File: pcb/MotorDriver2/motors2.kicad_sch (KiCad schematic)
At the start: 22 parts, among them Q2 IRLZ44NSTRLPBF, Q3 IRLZ44NSTRLPBF, Q4 IRLZ44NSTRLPBF, Q5 IRLZ44NSTRLPBF

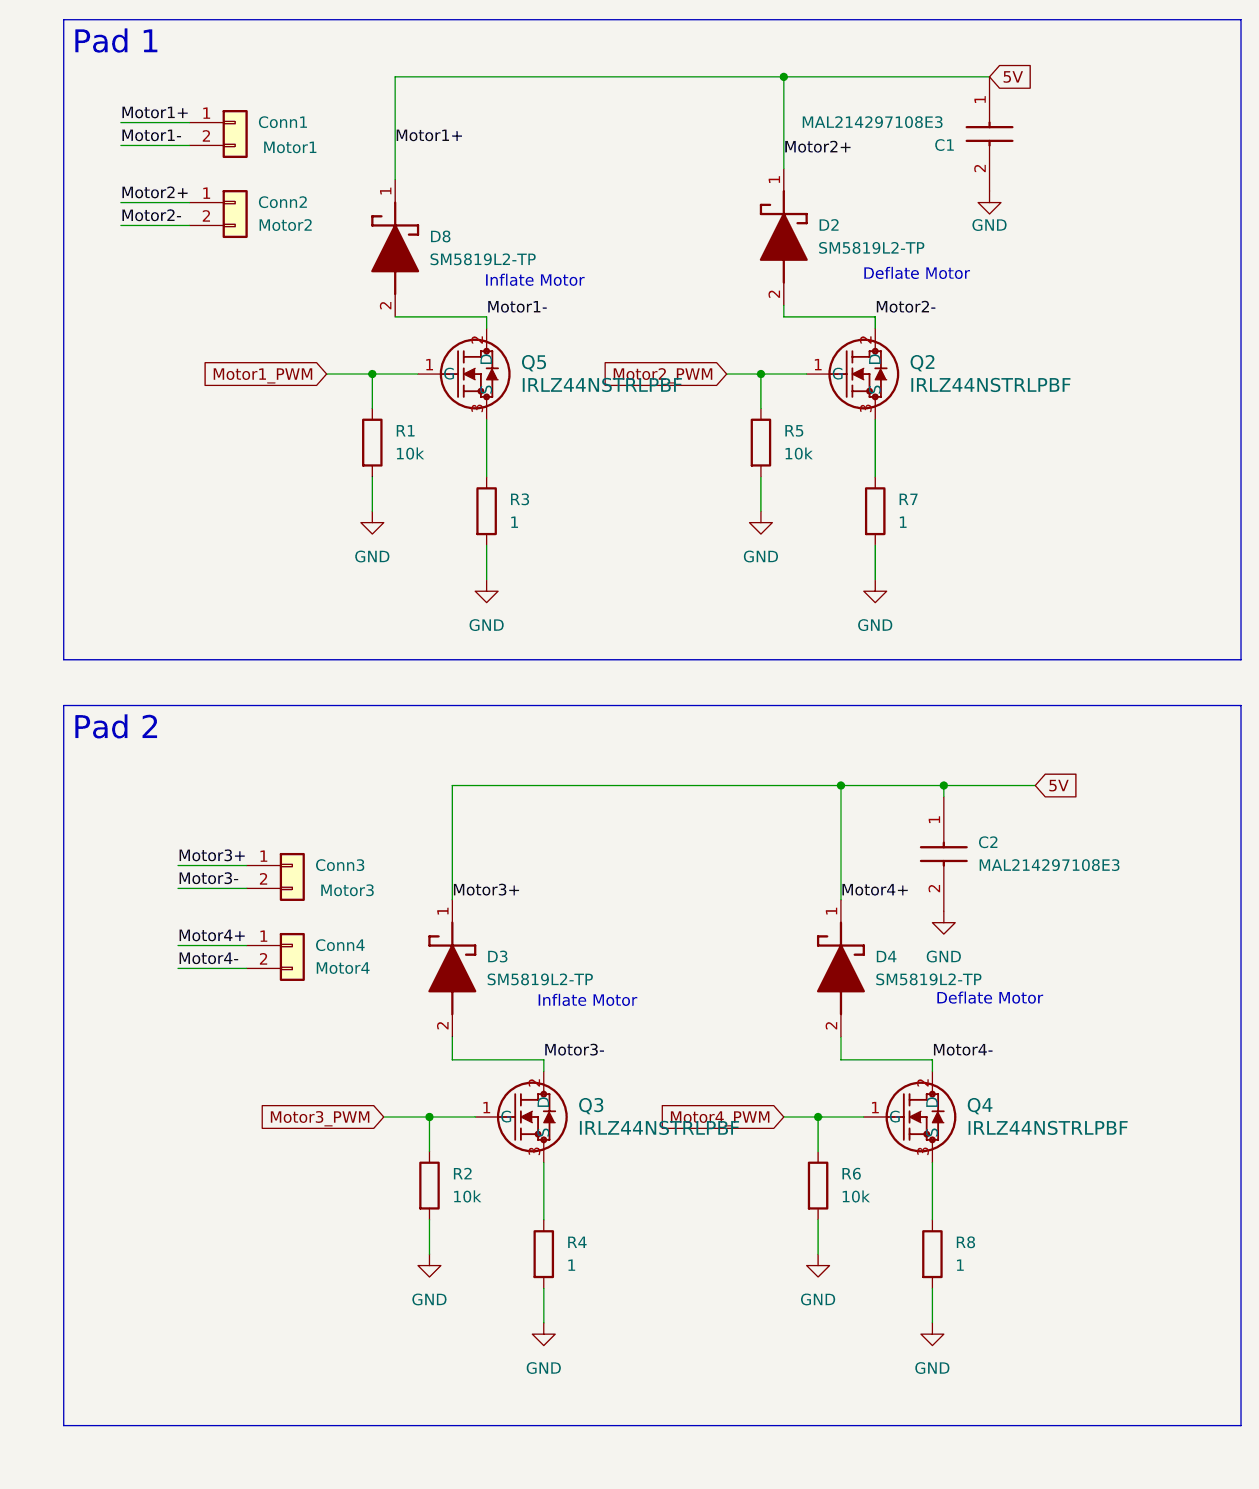
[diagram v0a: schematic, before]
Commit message: Modifying usb uart schematic
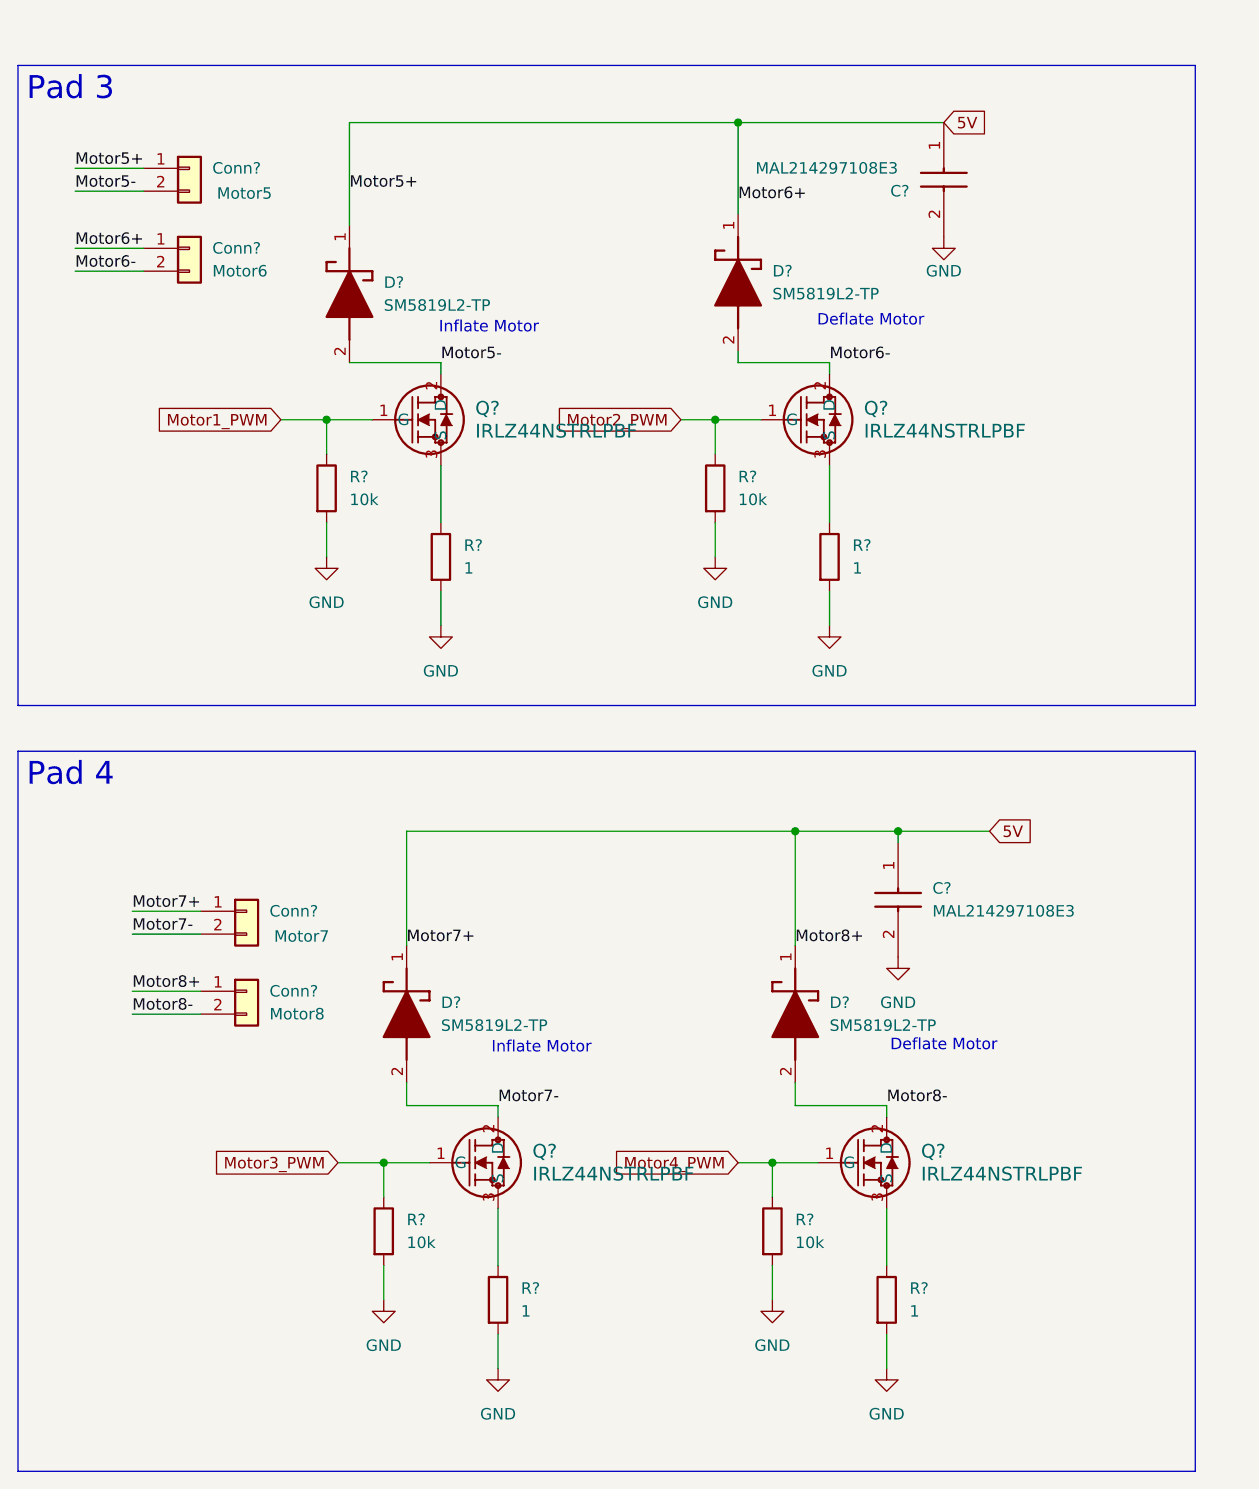
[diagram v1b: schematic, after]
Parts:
- removed C1, C2: MAL214297108E3, footprintLib:CAPAE680X800N, symbol pcb:MAL214297108E3
- removed Conn1: Motor1, Connector_PinHeader_2.54mm:PinHeader_1x02_P2.54mm_Vertical, symbol Connector_Generic:Conn_01x02
- removed Conn2: Motor2, Connector_PinHeader_2.54mm:PinHeader_1x02_P2.54mm_Vertical, symbol Connector_Generic:Conn_01x02
- removed Conn3: Motor3, Connector_PinHeader_2.54mm:PinHeader_1x02_P2.54mm_Vertical, symbol Connector_Generic:Conn_01x02
- removed Conn4: Motor4, Connector_PinHeader_2.54mm:PinHeader_1x02_P2.54mm_Vertical, symbol Connector_Generic:Conn_01x02
- removed D2, D3, D4, D8: SM5819L2-TP, footprintLib:SDO_SM5819L2-TP_MCE, symbol pcb:SM5819L2-TP
- removed Q2, Q3, Q4, Q5: IRLZ44NSTRLPBF, footprintLib:NMOSGDS_D2PAK_INF, symbol pcb:IRLZ44NSTRLPBF
- removed R1, R2, R5, R6: 10k, Resistor_SMD:R_0402_1005Metric, symbol Device:R
- removed R3, R4, R7, R8: 1, Resistor_SMD:R_1206_3216Metric, symbol Device:R
- added C? (x2): MAL214297108E3, footprintLib:CAPAE680X800N, symbol pcb:MAL214297108E3
- added Conn?: Motor8, Connector_PinHeader_2.54mm:PinHeader_1x02_P2.54mm_Vertical, symbol Connector_Generic:Conn_01x02
- added Conn?: Motor6, Connector_PinHeader_2.54mm:PinHeader_1x02_P2.54mm_Vertical, symbol Connector_Generic:Conn_01x02
- added Conn?: Motor5, Connector_PinHeader_2.54mm:PinHeader_1x02_P2.54mm_Vertical, symbol Connector_Generic:Conn_01x02
- added Conn?: Motor7, Connector_PinHeader_2.54mm:PinHeader_1x02_P2.54mm_Vertical, symbol Connector_Generic:Conn_01x02
- added D? (x4): SM5819L2-TP, footprintLib:SDO_SM5819L2-TP_MCE, symbol pcb:SM5819L2-TP
- added Q? (x4): IRLZ44NSTRLPBF, footprintLib:NMOSGDS_D2PAK_INF, symbol pcb:IRLZ44NSTRLPBF
- added R? (x4): 10k, Resistor_SMD:R_0402_1005Metric, symbol Device:R
- added R? (x4): 1, Resistor_SMD:R_1206_3216Metric, symbol Device:R
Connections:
- net 5V: now also C?.1 (+), C?.1 (+), Conn?.1 (Pin_1), Conn?.1 (Pin_1), Conn?.1 (Pin_1), Conn?.1 (Pin_1), D?.1 (K), D?.1 (K), D?.1 (K), D?.1 (K)
- net GND: now also C?.2 (-), C?.2 (-), R?.2, R?.2, R?.2, R?.2, R?.2, R?.2, R?.2, R?.2
- net Motor1_PWM: now also Q?.1 (G), R?.1
- net Motor2_PWM: now also Q?.1 (G), R?.1
- net Motor3_PWM: now also Q?.1 (G), R?.1
- net Motor4_PWM: now also Q?.1 (G), R?.1
- new net: Q?.3 (S), R?.1 (x4)
- new net Motor5-: Conn?.2 (Pin_2), D?.2 (A), Q?.2 (D)
- new net Motor6-: Conn?.2 (Pin_2), D?.2 (A), Q?.2 (D)
- new net Motor7-: Conn?.2 (Pin_2), D?.2 (A), Q?.2 (D)
- new net Motor8-: Conn?.2 (Pin_2), D?.2 (A), Q?.2 (D)

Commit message: Modified pwm pins
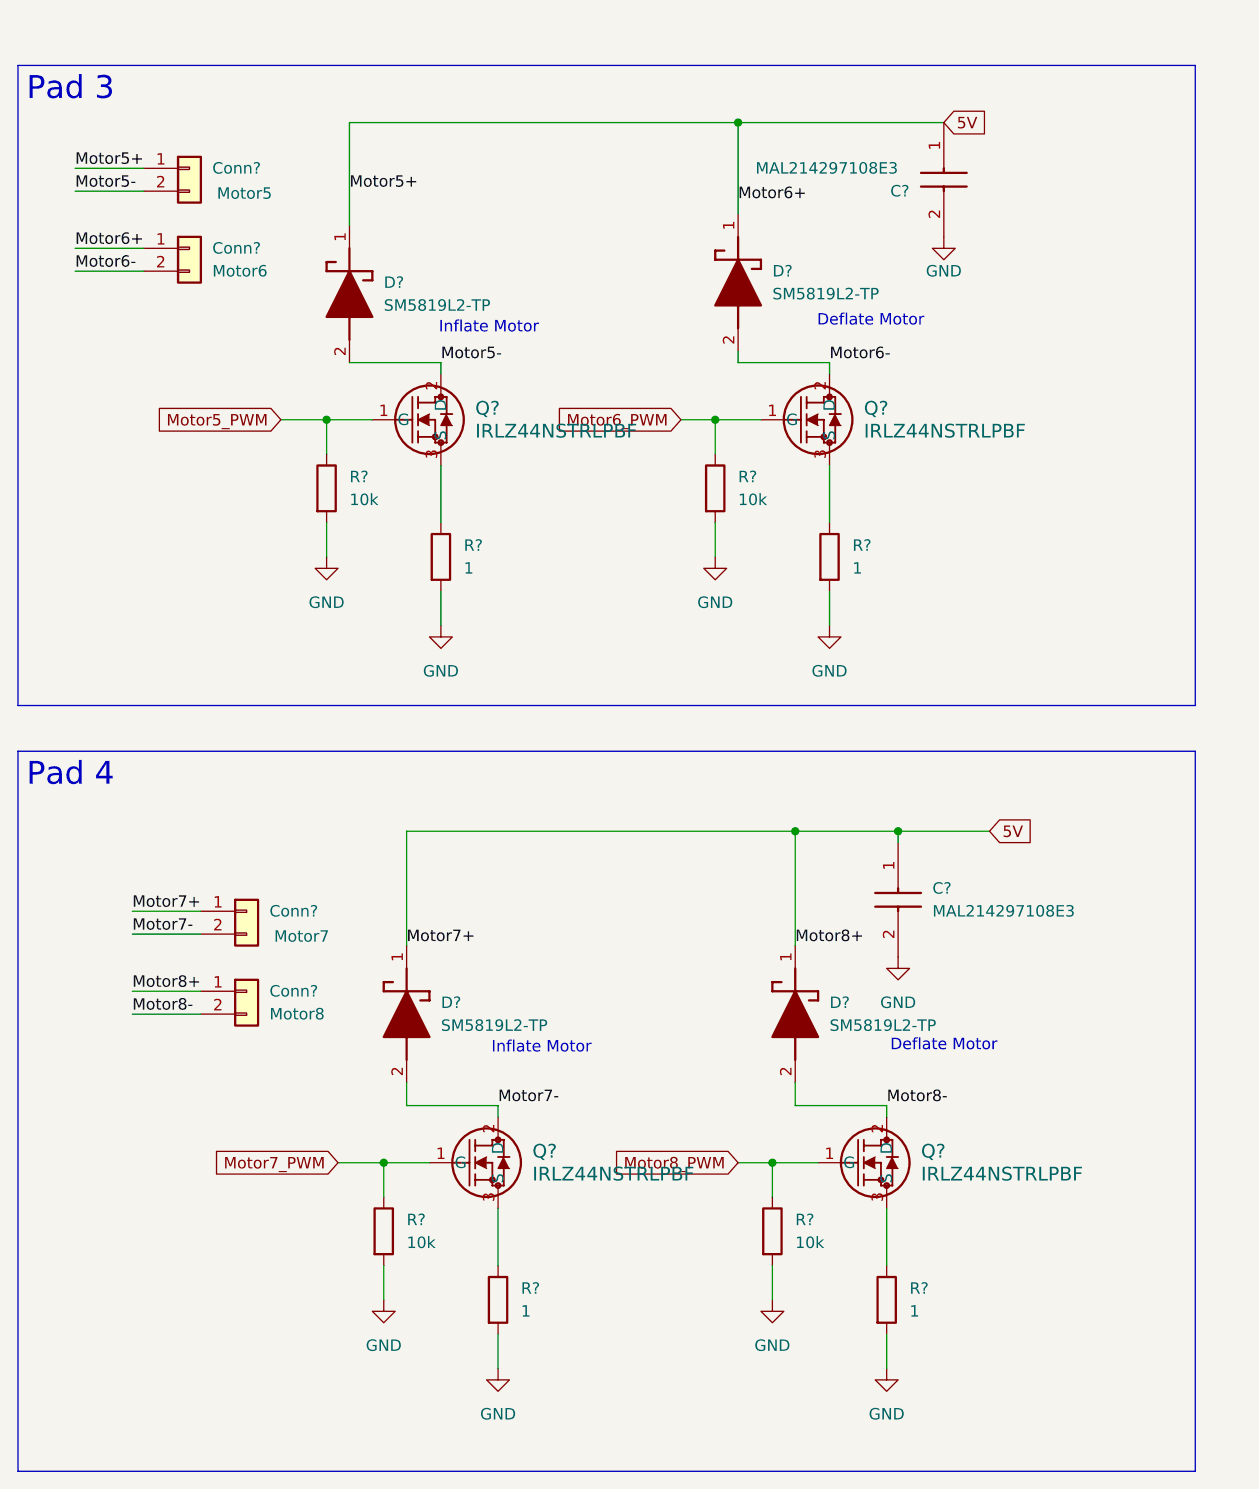
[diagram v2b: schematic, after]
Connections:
- net Motor1_PWM renamed Motor5_PWM
- net Motor2_PWM renamed Motor6_PWM
- net Motor3_PWM renamed Motor7_PWM
- net Motor4_PWM renamed Motor8_PWM
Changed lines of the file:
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@@
 		)
 	)
-	(global_label "Motor4_PWM"
+	(global_label "Motor8_PWM"
 		(shape input)
 		(at 107.95 149.86 180)
@@
 		)
 	)
-	(global_label "Motor3_PWM"
+	(global_label "Motor7_PWM"
 		(shape input)
 		(at 63.5 149.86 180)
@@
 		)
 	)
-	(global_label "Motor2_PWM"
+	(global_label "Motor6_PWM"
 		(shape input)
 		(at 101.6 67.31 180)
@@
 		)
 	)
-	(global_label "Motor1_PWM"
+	(global_label "Motor5_PWM"
 		(shape input)
 		(at 57.15 67.31 180)

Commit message: added ideal diode protection
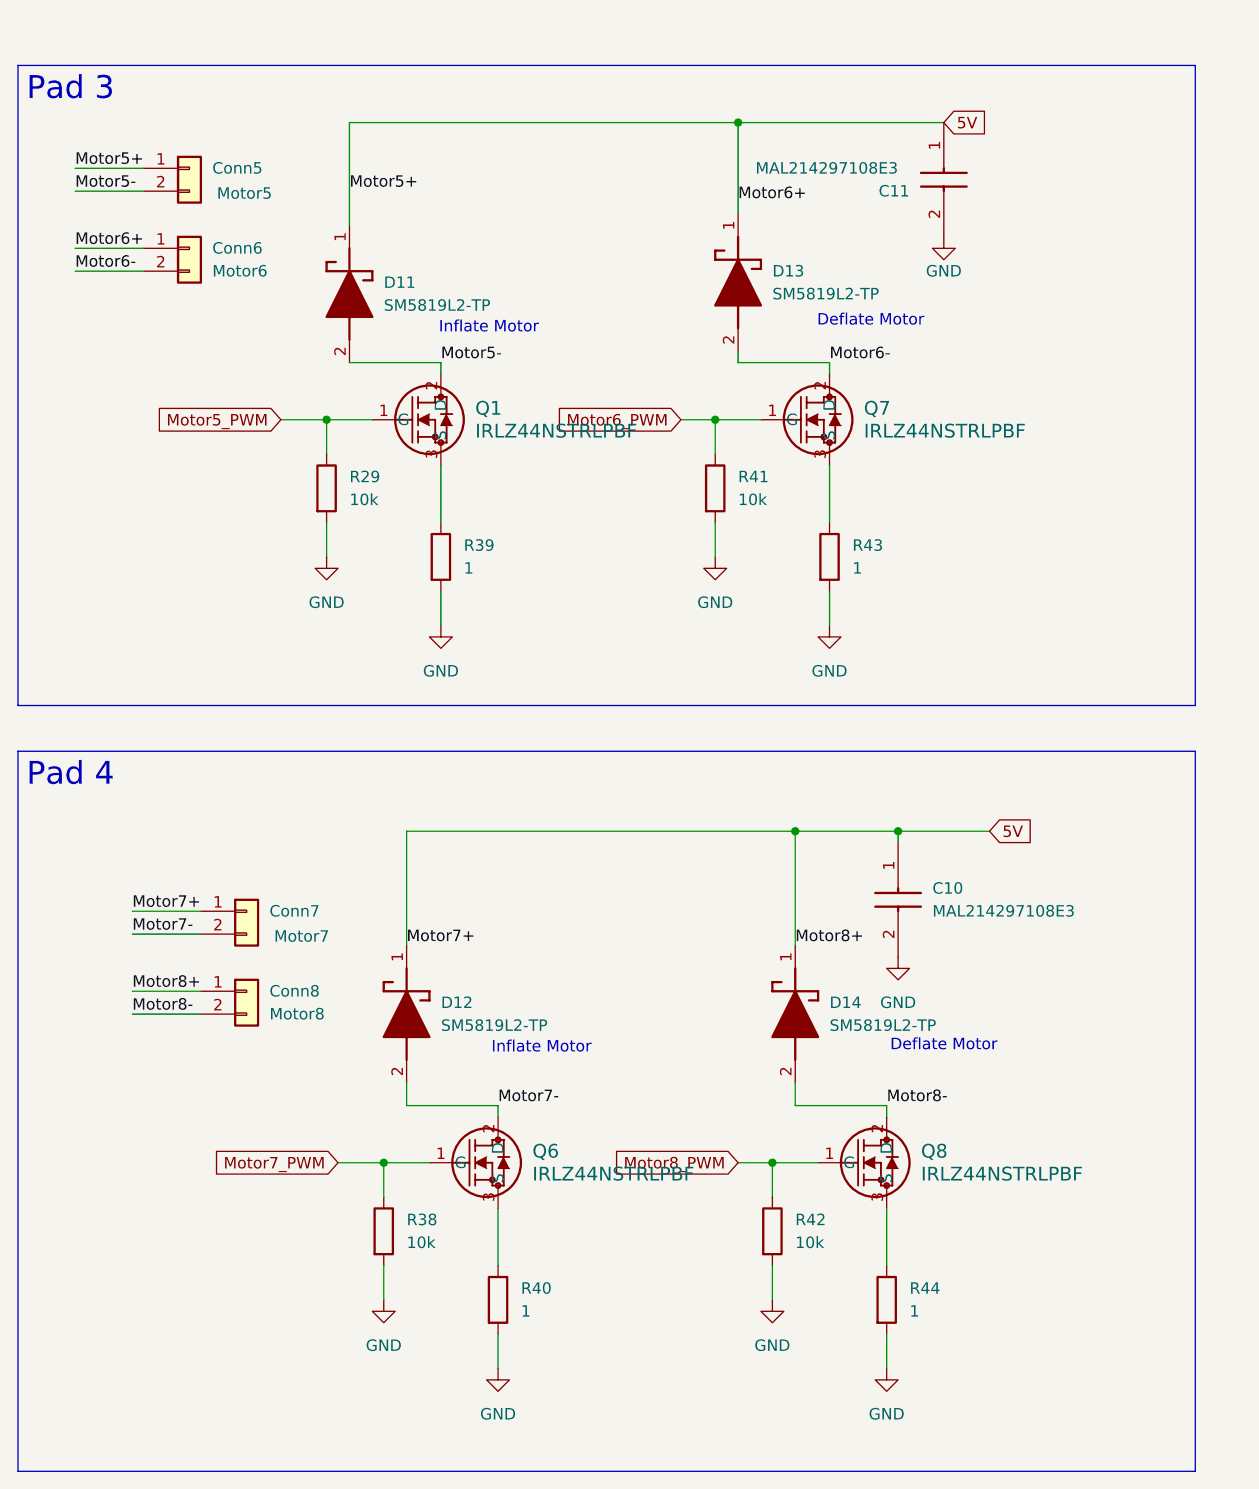
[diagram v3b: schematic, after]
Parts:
- gave numbers to parts that had none: 22

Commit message: Laying out PCB
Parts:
- removed D12: SM5819L2-TP, footprintLib:SDO_SM5819L2-TP_MCE, symbol pcb:SM5819L2-TP
- removed Q6: IRLZ44NSTRLPBF, footprintLib:NMOSGDS_D2PAK_INF, symbol pcb:IRLZ44NSTRLPBF
- removed R38: 10k, Resistor_SMD:R_0402_1005Metric, symbol Device:R
- removed R40: 1, Resistor_SMD:R_1206_3216Metric, symbol Device:R
- added D8: SM5819L2-TP, CapstoneFootprints:SDO_SM5819L2-TP_MCE, symbol pcb:SM5819L2-TP
- added Q5: IRLZ44NSTRLPBF, CapstoneFootprints:NMOSGDS_D2PAK_INF, symbol pcb:IRLZ44NSTRLPBF
- added R1: 10k, Resistor_SMD:R_0402_1005Metric, symbol Device:R
- added R3: 1, Resistor_SMD:R_1206_3216Metric, symbol Device:R
- C10, C11: value MAL214297108E3 -> Honor Elec RVT1H470M0607; footprint footprintLib:CAPAE680X800N -> CapstoneFootprints:CAPAE680X800N
- D11, D13, D14: footprint footprintLib:SDO_SM5819L2-TP_MCE -> CapstoneFootprints:SDO_SM5819L2-TP_MCE
- Q1, Q7, Q8: footprint footprintLib:NMOSGDS_D2PAK_INF -> CapstoneFootprints:NMOSGDS_D2PAK_INF
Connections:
- net 5V: now also D8.1 (K)
- net GND: now also R1.2, R3.2
- net Motor5- renamed Motor3a-
- net Motor5_PWM renamed Motor3a_PWM
- net Motor6- renamed Motor3b-
- net Motor6_PWM renamed Motor3b_PWM
- net Motor7- renamed Motor4a-
- net Motor4a-: now also D8.2 (A), Q5.2 (D)
- net Motor8- renamed Motor4b-
- net Motor8_PWM renamed Motor4b_PWM
- new net: Q5.3 (S), R3.1
- new net Motor4a_PWM: Q5.1 (G), R1.1
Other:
- moved on the sheet: Conn7, Conn8
